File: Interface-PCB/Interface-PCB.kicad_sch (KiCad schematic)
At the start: 17 parts, among them J1 BARREL_JACK_PAD, J2 BARREL_JACK_PAD, J3 GPIO_DEBUG_HEADER, J4 RASPBERRYPI_GPIO_CONN_HEADER, M1 PERISTALTIC_PUMP, M2 PERISTALTIC_PUMP, M3 PERISTALTIC_PUMP, U1 TB6612FNG_BREAKOUT, U2 TB6612FNG_BREAKOUT

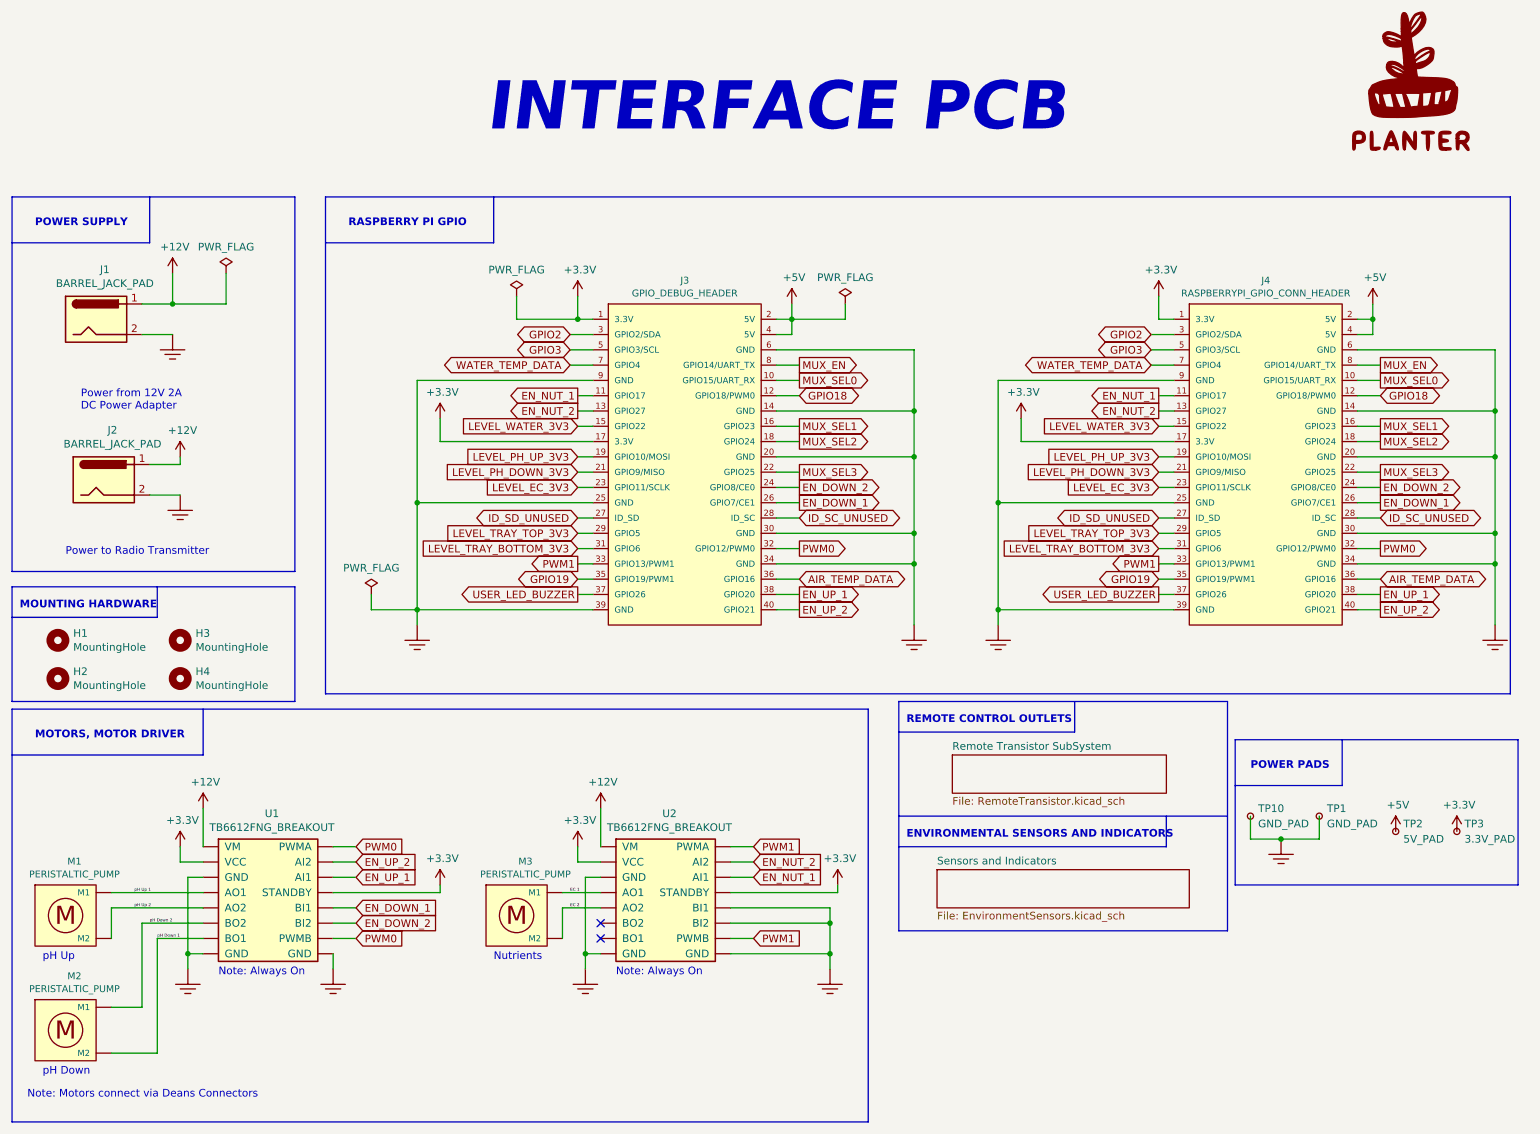
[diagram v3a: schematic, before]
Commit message: Complete PCB layout
- Complete component positioning and PCB layout
- Swap most pin assignments to resolve track route criss-crossing
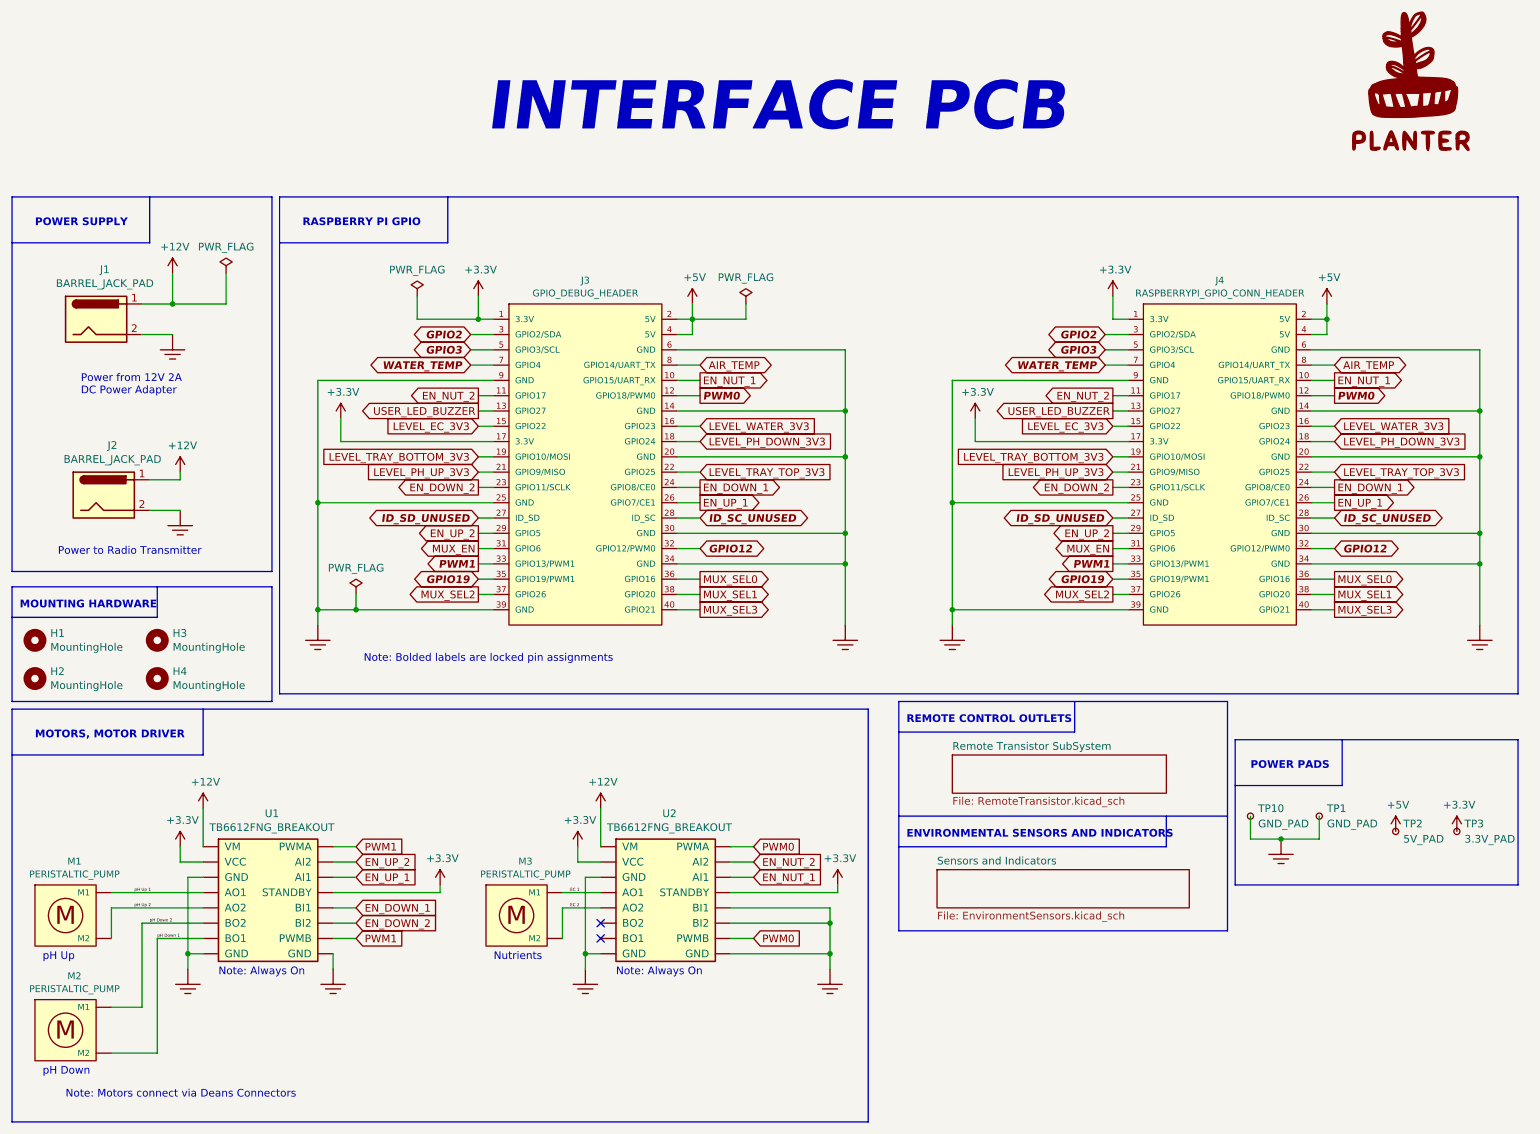
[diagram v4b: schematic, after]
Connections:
- net AIR_TEMP_DATA is gone; now on net MUX_SEL0: J3.36 (GPIO16), J4.36 (GPIO16)
- net GPIO18 is gone; now on net PWM0: J3.12 (GPIO18/PWM0), J4.12 (GPIO18/PWM0)
- net EN_DOWN_1: now also J3.24 (GPIO8/CE0), J4.24 (GPIO8/CE0); no longer J3.26 (GPIO7/CE1), J4.26 (GPIO7/CE1)
- net EN_DOWN_2: now also J3.23 (GPIO11/SCLK), J4.23 (GPIO11/SCLK); no longer J3.24 (GPIO8/CE0), J4.24 (GPIO8/CE0)
- net EN_NUT_1: now also J3.10 (GPIO15/UART_RX), J4.10 (GPIO15/UART_RX); no longer J3.11 (GPIO17), J4.11 (GPIO17)
- net EN_NUT_2: now also J3.11 (GPIO17), J4.11 (GPIO17); no longer J3.13 (GPIO27), J4.13 (GPIO27)
- net EN_UP_1: now also J3.26 (GPIO7/CE1), J4.26 (GPIO7/CE1); no longer J3.38 (GPIO20), J4.38 (GPIO20)
- net EN_UP_2: now also J3.29 (GPIO5), J4.29 (GPIO5); no longer J3.40 (GPIO21), J4.40 (GPIO21)
- net LEVEL_EC_3V3: now also J3.15 (GPIO22), J4.15 (GPIO22); no longer J3.23 (GPIO11/SCLK), J4.23 (GPIO11/SCLK)
- net LEVEL_PH_DOWN_3V3: now also J3.18 (GPIO24), J4.18 (GPIO24); no longer J3.21 (GPIO9/MISO), J4.21 (GPIO9/MISO)
- net LEVEL_PH_UP_3V3: now also J3.21 (GPIO9/MISO), J4.21 (GPIO9/MISO); no longer J3.19 (GPIO10/MOSI), J4.19 (GPIO10/MOSI)
- net LEVEL_TRAY_BOTTOM_3V3: now also J3.19 (GPIO10/MOSI), J4.19 (GPIO10/MOSI); no longer J3.31 (GPIO6), J4.31 (GPIO6)
- net LEVEL_TRAY_TOP_3V3: now also J3.22 (GPIO25), J4.22 (GPIO25); no longer J3.29 (GPIO5), J4.29 (GPIO5)
- net LEVEL_WATER_3V3: now also J3.16 (GPIO23), J4.16 (GPIO23); no longer J3.15 (GPIO22), J4.15 (GPIO22)
- net MUX_EN: now also J3.31 (GPIO6), J4.31 (GPIO6); no longer J3.8 (GPIO14/UART_TX), J4.8 (GPIO14/UART_TX)
- net MUX_SEL0: no longer J3.10 (GPIO15/UART_RX), J4.10 (GPIO15/UART_RX)
- net MUX_SEL1: now also J3.38 (GPIO20), J4.38 (GPIO20); no longer J3.16 (GPIO23), J4.16 (GPIO23)
- net MUX_SEL2: now also J3.37 (GPIO26), J4.37 (GPIO26); no longer J3.18 (GPIO24), J4.18 (GPIO24)
- net MUX_SEL3: now also J3.40 (GPIO21), J4.40 (GPIO21); no longer J3.22 (GPIO25), J4.22 (GPIO25)
- net PWM0: now also U2.15 (PWMB), U2.9 (PWMA); no longer J3.32 (GPIO12/PWM0), J4.32 (GPIO12/PWM0), U1.15 (PWMB), U1.9 (PWMA)
- net PWM1: now also U1.15 (PWMB), U1.9 (PWMA); no longer U2.15 (PWMB), U2.9 (PWMA)
- net USER_LED_BUZZER: now also J3.13 (GPIO27), J4.13 (GPIO27); no longer J3.37 (GPIO26), J4.37 (GPIO26)
- net WATER_TEMP_DATA renamed WATER_TEMP
- new net AIR_TEMP: J3.8 (GPIO14/UART_TX), J4.8 (GPIO14/UART_TX)
- new net GPIO12: J3.32 (GPIO12/PWM0), J4.32 (GPIO12/PWM0)
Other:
- note added: "Note: Bolded labels are locked pin assignments"
- moved on the sheet: H1, H2, H3, H4, J2, J3, J4
